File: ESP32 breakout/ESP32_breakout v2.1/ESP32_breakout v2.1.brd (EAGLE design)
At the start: 88.9 x 83.8 mm, 48 parts, among them Q1 BSS84, Q2 BSS84, U1 ESP-WROOM-32, U2 NCP-1117, Y1 12MHz

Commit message: Added USB bypass cap and extra status LED
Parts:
- added C18: 0.1uF, dr-library:CAP-0603
- added D6: (no value), dr-library:LED-1206
- added J2: JUMPER_2-WAY, dr-library:1X02
- added Q3: BSS84, dr-library:SOT-23-3
- added R7: 330, dr-library:RES-0805
- moved Q1 4.02 mm to (61.6, 26.7)
- moved Q2 3.42 mm to (61.6, 22.2)
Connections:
- new net HEART: J2.1, Q3.G
- new net N$10: Q3.D, R7.2
- new net N$9: D6.A, R7.1
- net +3V3: now also Q3.S
- net GND: now also C18.2, D6.C
- net IO19: now also J2.2
- net VCC: now also C18.1
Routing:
- net IO19: track 12.5 -> 70.8 mm
- net HEART: track 0.00 -> 5.54 mm
- net N$9: track 0.00 -> 3.94 mm
- net GND: track 197.7 -> 201.3 mm, vias 192 -> 191
- net N$10: track 0.00 -> 3.29 mm
- net +3V3: track 263.8 -> 261.4 mm, vias 21 -> 20
- net TX: track 111.4 -> 109.1 mm
- net VCC: track 120.7 -> 122.6 mm
- net RX: track 101.2 -> 100.0 mm
- net N$6: track 16.5 -> 15.4 mm

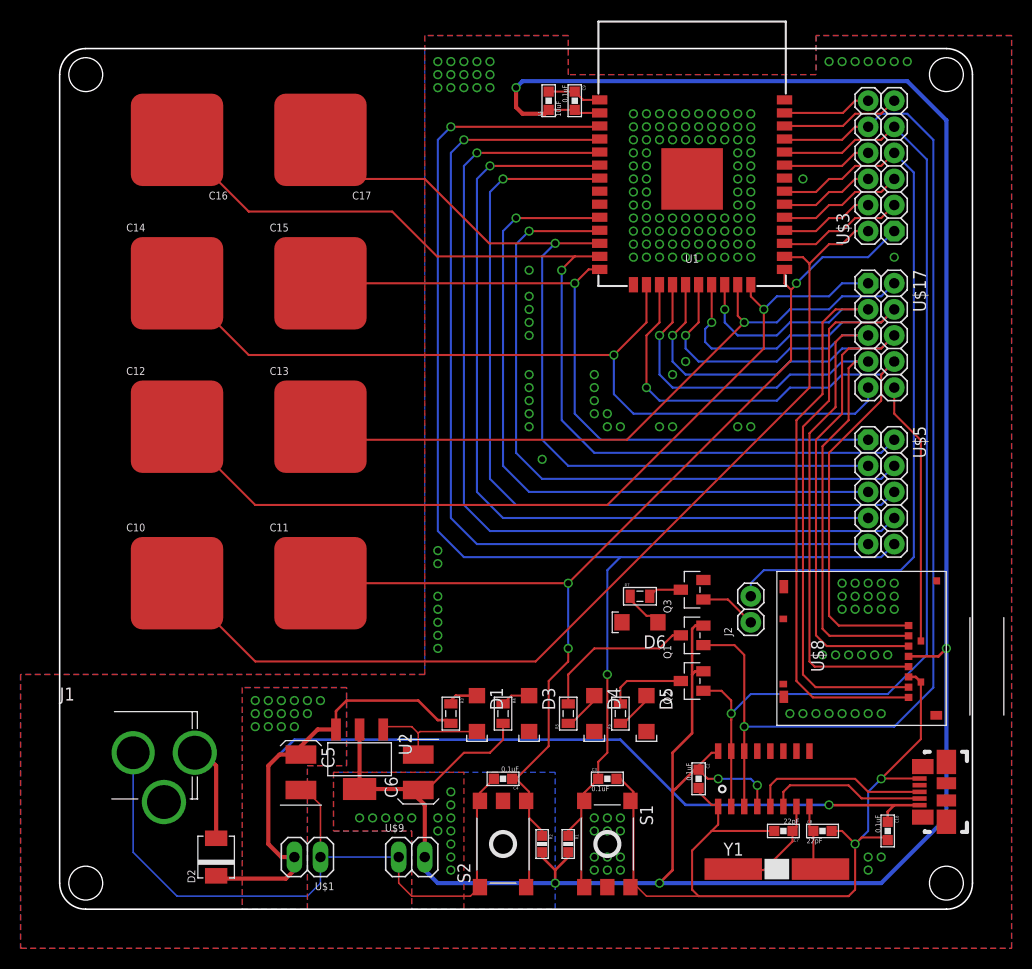
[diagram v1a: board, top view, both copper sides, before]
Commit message: Modified labels
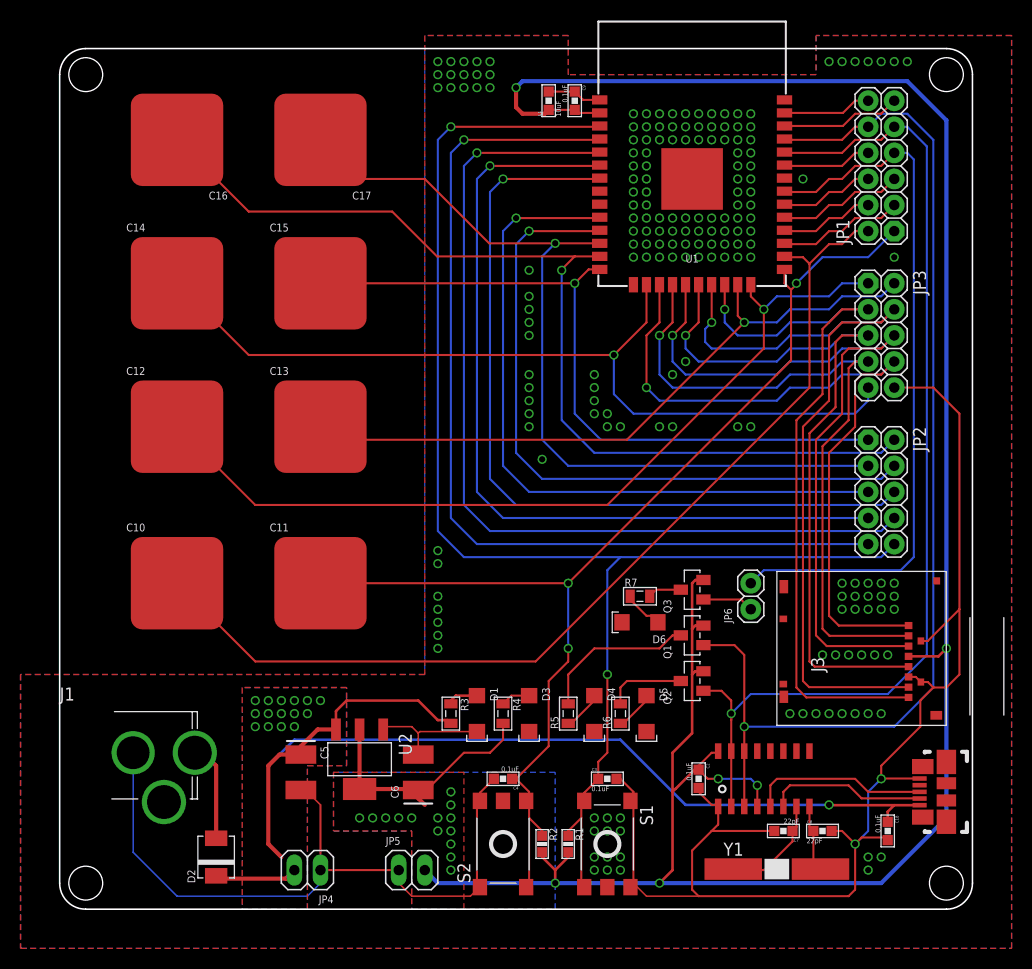
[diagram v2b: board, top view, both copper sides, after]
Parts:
- removed J2: JUMPER_2-WAY, dr-library:1X02
- removed U$1, U$9: M02LONG, dr-library:1X02-LONG
- added JP4, JP5: M02LONG, dr-library:1X02-LONG
- added JP6: JUMPER_2-WAY, dr-library:1X02
- renumbered U$17 to JP3, U$3 to JP1, U$5 to JP2, U$8 to J3
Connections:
- net +3V3: now also JP5.2; no longer U$9.2
- net GND: now also JP4.1, JP5.1; no longer U$1.1, U$9.1
- net HEART: now also JP6.1; no longer J2.1
- net IO19: now also JP6.2; no longer J2.2
- net VCC: now also JP4.2; no longer U$1.2
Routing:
- net GND: track 201.3 -> 215.3 mm
- net VCC: track 122.6 -> 118.8 mm
- net SD2: track 72.3 -> 73.4 mm
- net RX: track 100.0 -> 100.7 mm
- net +3V3: track 261.4 -> 260.8 mm
- net IO19: track 70.8 -> 70.3 mm
- net HEART: track 5.54 -> 5.01 mm

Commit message: DRU check
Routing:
- net TX: track 109.1 -> 109.6 mm
- net RX: track 100.7 -> 101.2 mm
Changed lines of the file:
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@@
 <wire x1="82.55" y1="77.47" x2="80.01" y2="77.47" width="0.2032" layer="16"/>
 <contactref element="Q1" pad="G"/>
-<wire x1="66.675" y1="10.005" x2="66.675" y2="17.78" width="0.2032" layer="1"/>
 <wire x1="66.675" y1="17.78" x2="66.675" y2="24.765" width="0.2032" layer="1"/>
 <via x="66.675" y="17.78" extent="1-16" drill="0.6"/>
@@
 <wire x1="77.47" y1="76.2" x2="78.74" y2="76.2" width="0.2032" layer="1"/>
 <wire x1="80.01" y1="77.47" x2="78.74" y2="76.2" width="0.2032" layer="16"/>
+<wire x1="66.675" y1="17.78" x2="66.675" y2="17.145" width="0.2032" layer="1"/>
+<wire x1="66.675" y1="17.145" x2="67.31" y2="16.51" width="0.2032" layer="1"/>
+<wire x1="67.31" y1="16.51" x2="67.31" y2="13.335" width="0.2032" layer="1"/>
+<wire x1="67.31" y1="13.335" x2="66.675" y2="12.7" width="0.2032" layer="1"/>
+<wire x1="66.675" y1="12.7" x2="66.675" y2="10.005" width="0.2032" layer="1"/>
 </signal>
 <signal name="RX">
@@
 <wire x1="84.455" y1="24.765" x2="84.455" y2="74.295" width="0.2032" layer="16"/>
 <contactref element="Q2" pad="G"/>
-<wire x1="65.405" y1="10.005" x2="65.405" y2="19.05" width="0.2032" layer="1"/>
 <wire x1="65.405" y1="19.05" x2="65.405" y2="18.415" width="0.2032" layer="1"/>
 <wire x1="67.31" y1="20.955" x2="65.405" y2="19.05" width="0.2032" layer="16"/>
@@
 <wire x1="84.455" y1="74.295" x2="82.55" y2="76.2" width="0.2032" layer="16"/>
 <wire x1="82.55" y1="76.2" x2="81.28" y2="76.2" width="0.2032" layer="16"/>
+<wire x1="65.405" y1="19.05" x2="65.405" y2="17.145" width="0.2032" layer="1"/>
+<wire x1="65.405" y1="17.145" x2="66.04" y2="16.51" width="0.2032" layer="1"/>
+<wire x1="66.04" y1="16.51" x2="66.04" y2="13.335" width="0.2032" layer="1"/>
+<wire x1="66.04" y1="13.335" x2="65.405" y2="12.7" width="0.2032" layer="1"/>
+<wire x1="65.405" y1="12.7" x2="65.405" y2="10.005" width="0.2032" layer="1"/>
 </signal>
 <signal name="IO14/T6">

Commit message: gerber generated
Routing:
- net GND: vias 191 -> 192
- net +3V3: vias 20 -> 19
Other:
- board outline removed
- board text added: "3V3"
- board text added: "5V"
- board text added: "BOOT"
- board text added: "CLK"
- board text added: "CMD"
- board text added: "EN"
- board text added: "ESP32 Breakout 13 June 2017 v2.0 D. Rances"
- board text added: "ESP32 Breakout v2.0 D. Rances"
- board text added: "GND"
- board text added: "HEARTBEAT JMPR"
- board text added: "IO0"
- board text added: "IO12"
- board text added: "IO13"
- board text added: "IO14"
- board text added: "IO15"
- board text added: "IO16"
- board text added: "IO17"
- board text added: "IO18"
- board text added: "IO19"
- board text added: "IO19 HEART"
- board text added: "IO2"
- board text added: "IO21"
- board text added: "IO22"
- board text added: "IO23"
- board text added: "IO25"
- board text added: "IO26"
- board text added: "IO27"
- board text added: "IO34"
- board text added: "IO35"
- board text added: "IO4"
- board text added: "IO5"
- board text added: "RESET"
- board text added: "RX"
- board text added: "SD0"
- board text added: "SD1"
- board text added: "SD2"
- board text added: "SD3"
- board text added: "SVN"
- board text added: "SVP"
- board text added: "T0"
- board text added: "T1"
- board text added: "T2"
- board text added: "T3"
- board text added: "T4"
- board text added: "T5"
- board text added: "T6"
- board text added: "T7"
- board text added: "TX"
- board text added: "U3"
- board text added: "V+"
